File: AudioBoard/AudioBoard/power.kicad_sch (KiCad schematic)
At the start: 3 parts, among them J7 Barrel_Jack, SW3 PWR_SW

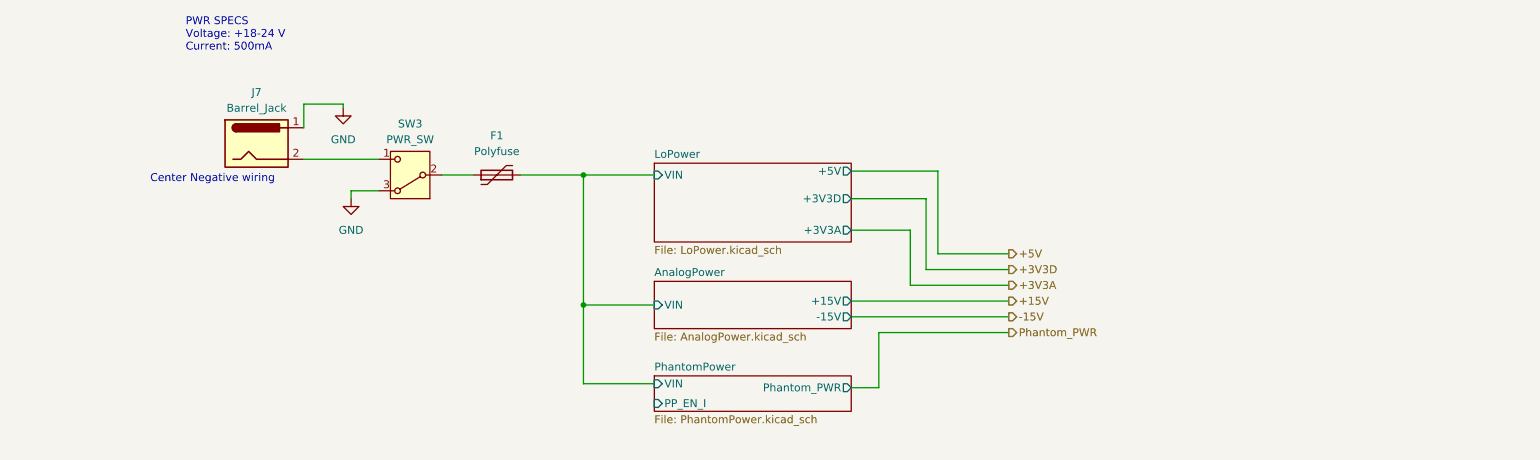
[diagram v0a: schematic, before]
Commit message: added power protection, dcdc modules
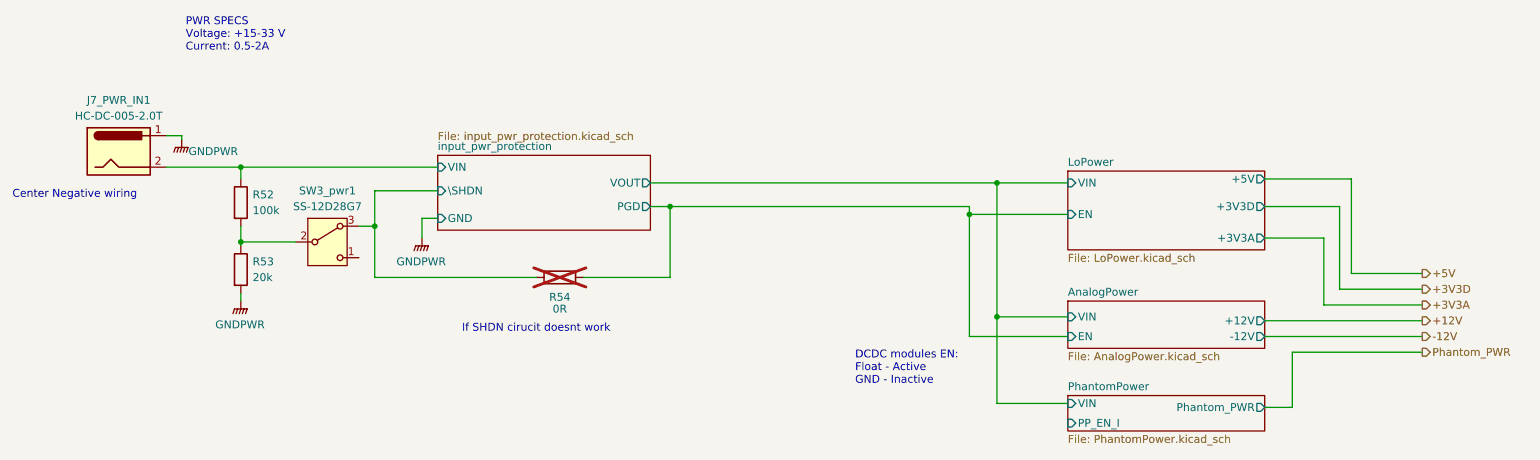
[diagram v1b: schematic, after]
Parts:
- removed F1: Polyfuse, symbol Device:Polyfuse
- added R52: 100k, symbol Device:R
- added R53: 20k, symbol Device:R
- added R54: 0R, symbol Device:R
- J7_PWR_IN1: renamed from J7; value Barrel_Jack -> HC-DC-005-2.0T
- SW3_pwr1: renamed from SW3; value PWR_SW -> SS-12D28G7
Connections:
- net at SW3_pwr1.2 (B): now also R52.2, R53.1
- net at SW3_pwr1.1 (C): no longer J7_PWR_IN1.2
- net GND renamed GNDPWR
- net GNDPWR: now also R53.2; no longer SW3_pwr1.3 (A)
- new net AnalogPower/EN: R54.1
- new net input_pwr_protection/VIN: J7_PWR_IN1.2, R52.1
- new net input_pwr_protection/\SHDN: R54.2, SW3_pwr1.3 (A)
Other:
- added sheet input_pwr_protection (input_pwr_protection.kicad_sch)
- sheet AnalogPower ports: added +12V, -12V, EN; removed +15V, -15V
- sheet LoPower ports: added EN; removed none
- note added: "DCDC modules EN: Float - Active GND - Inactive"
- note added: "If SHDN cirucit doesnt work"
- note added: "PWR SPECS Voltage: +15-33 V Current: 0.5-2A"
- note removed: "PWR SPECS Voltage: +18-24 V Current: 500mA"
- moved on the sheet: J7_PWR_IN1, SW3_pwr1

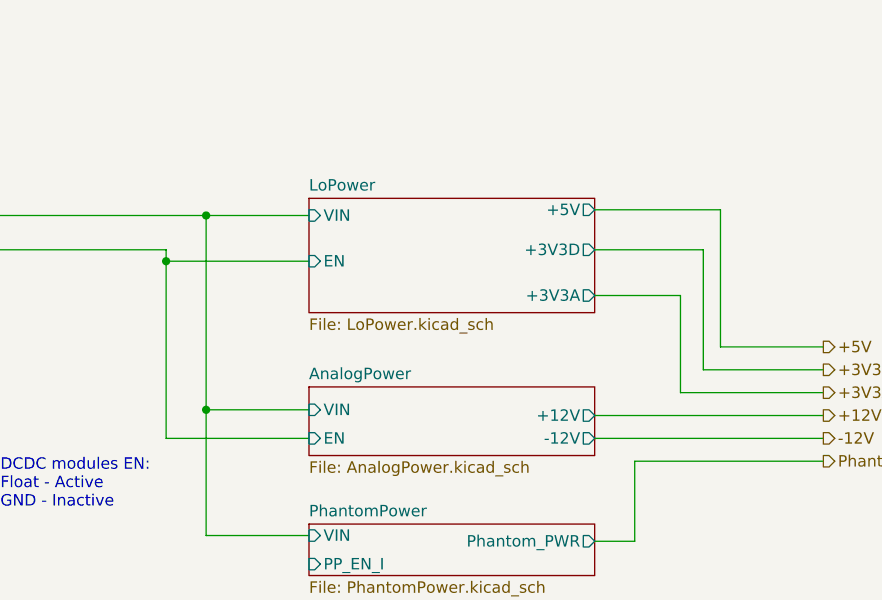
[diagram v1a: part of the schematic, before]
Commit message: assigned footprint to elements lcsc parts
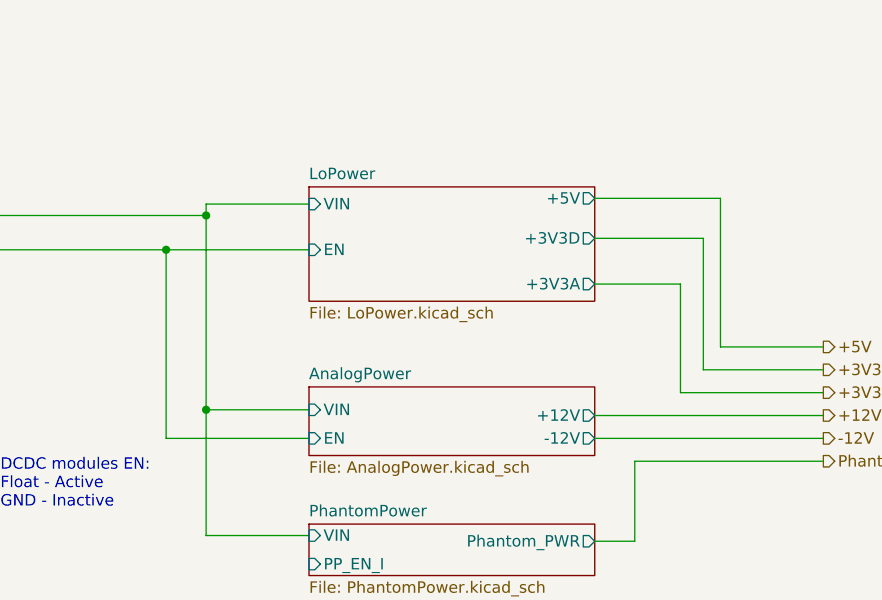
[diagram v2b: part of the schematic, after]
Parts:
- R52: footprint (none) -> Resistor_SMD:R_0402_1005Metric; JLCPCB (none) -> C25741; LCSC Part (none) -> C25741
- R53: footprint (none) -> Resistor_SMD:R_0603_1608Metric; JLCPCB (none) -> C4184; LCSC Part (none) -> C4184
- R54: footprint (none) -> Resistor_SMD:R_0603_1608Metric_Pad0.98x0.95mm_HandSolder; JLCPCB (none) -> C21189; LCSC Part (none) -> C21189
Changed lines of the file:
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@@
+	)
+	(junction
+		(at 174.625 43.815)
+		(diameter 0)
+		(color 0 0 0 0)
 	)
 	(junction
@@
 	)
 	(junction
-		(at 174.625 45.085)
-		(diameter 0)
-		(color 0 0 0 0)
-	)
-	(junction
 		(at 179.07 61.595)
 		(diameter 0)
@@
 	(wire
 		(pts
+			(xy 179.07 38.735) (xy 179.07 40.005)
+		)
+		(stroke
+			(width 0)
+			(type default)
+		)
+	)
+	(wire
+		(pts
 			(xy 57.15 37.465) (xy 57.15 39.37)
 		)
@@
 	(wire
 		(pts
-			(xy 234.315 43.815) (xy 234.315 57.15)
-		)
-		(stroke
-			(width 0)
-			(type default)
-		)
-	)
-	(wire
-		(pts
-			(xy 190.5 45.085) (xy 174.625 45.085)
+			(xy 174.625 43.815) (xy 174.625 64.77)
+		)
+		(stroke
+			(width 0)
+			(type default)
+		)
+	)
+	(wire
+		(pts
+			(xy 234.315 42.545) (xy 234.315 57.15)
+		)
+		(stroke
+			(width 0)
+			(type default)
+		)
+	)
+	(wire
+		(pts
+			(xy 190.5 43.815) (xy 174.625 43.815)
 		)
 		(stroke
@@
 	(wire
 		(pts
-			(xy 236.22 39.37) (xy 222.25 39.37)
+			(xy 236.22 38.1) (xy 222.25 38.1)
 		)
 		(stroke
@@
 	(wire
 		(pts
-			(xy 174.625 45.085) (xy 174.625 64.77)
-		)
-		(stroke
-			(width 0)
-			(type default)
-		)
-	)
-	(wire
-		(pts
-			(xy 174.625 43.815) (xy 174.625 45.085)
-		)
-		(stroke
-			(width 0)
-			(type default)
-		)
-	)
-	(wire
-		(pts
 			(xy 126.365 43.815) (xy 174.625 43.815)
 		)
@@
 	(wire
 		(pts
-			(xy 222.25 43.815) (xy 234.315 43.815)
+			(xy 222.25 42.545) (xy 234.315 42.545)
 		)
 		(stroke
@@
 	(wire
 		(pts
-			(xy 222.25 48.895) (xy 231.775 48.895)
+			(xy 222.25 47.625) (xy 231.775 47.625)
 		)
 		(stroke
@@
 	(wire
 		(pts
-			(xy 179.07 40.005) (xy 190.5 40.005)
+			(xy 179.07 38.735) (xy 190.5 38.735)
 		)
 		(stroke
@@
 	(wire
 		(pts
-			(xy 236.22 54.61) (xy 236.22 39.37)
-		)
-		(stroke
-			(width 0)
-			(type default)
-		)
-	)
-	(wire
-		(pts
-			(xy 231.775 48.895) (xy 231.775 59.69)
+			(xy 236.22 54.61) (xy 236.22 38.1)
+		)
+		(stroke
+			(width 0)
+			(type default)
+		)
+	)
+	(wire
+		(pts
+			(xy 231.775 47.625) (xy 231.775 59.69)
 		)
 		(stroke
@@
 			)
 		)
-		(property "Footprint" ""
+		(property "Footprint" "Resistor_SMD:R_0402_1005Metric"
 			(at 55.372 43.18 90)
 			(hide yes)
@@
 		)
 		(property "Description" "Resistor"
+			(at 57.15 43.18 0)
+			(hide yes)
+			(show_name no)
+			(do_not_autoplace no)
+			(effects
+				(font
+					(size 1.27 1.27)
+				)
+			)
+		)
+		(property "I" ""
+			(at 57.15 43.18 0)
+			(hide yes)
+			(show_name no)
+			(do_not_autoplace no)
+			(effects
+				(font
+					(size 1.27 1.27)
+				)
+			)
+		)
+		(property "JLCPCB" "C25741"
+			(at 57.15 43.18 0)
+			(hide yes)
+			(show_name no)
+			(do_not_autoplace no)
+			(effects
+				(font
+					(size 1.27 1.27)
+				)
+			)
+		)
+		(property "LCSC Part" "C25741"
+			(at 57.15 43.18 0)
+			(hide yes)
+			(show_name no)
+			(do_not_autoplace no)
+			(effects
+				(font
+					(size 1.27 1.27)
+				)
+			)
+		)
+		(property "esr" ""
 			(at 57.15 43.18 0)
 			(hide yes)
@@
 			)
 		)
-		(property "Footprint" ""
+		(property "Footprint" "Resistor_SMD:R_0603_1608Metric"
 			(at 55.372 53.975 90)
 			(hide yes)
@@
 		)
 		(property "Description" "Resistor"
+			(at 57.15 53.975 0)
+			(hide yes)
+			(show_name no)
+			(do_not_autoplace no)
+			(effects
+				(font
+					(size 1.27 1.27)
+				)
+			)
+		)
+		(property "I" ""
+			(at 57.15 53.975 0)
+			(hide yes)
+			(show_name no)
+			(do_not_autoplace no)
+			(effects
+				(font
+					(size 1.27 1.27)
+				)
+			)
+		)
+		(property "JLCPCB" "C4184"
+			(at 57.15 53.975 0)
+			(hide yes)
+			(show_name no)
+			(do_not_autoplace no)
+			(effects
+				(font
+					(size 1.27 1.27)
+				)
+			)
+		)
+		(property "LCSC Part" "C4184"
+			(at 57.15 53.975 0)
+			(hide yes)
+			(show_name no)
+			(do_not_autoplace no)
+			(effects
+				(font
+					(size 1.27 1.27)
+				)
+			)
+		)
+		(property "esr" ""
 			(at 57.15 53.975 0)
 			(hide yes)
@@
 			)
 		)
-		(property "Footprint" ""
+		(property "Footprint" "Resistor_SMD:R_0603_1608Metric_Pad0.98x0.95mm_HandSolder"
 			(at 108.585 53.467 90)
 			(hide yes)
@@
 		(property "Description" "Resistor"
 			(at 108.585 55.245 0)
+			(hide yes)
+			(show_name no)
+			(do_not_autoplace no)
+			(effects
+				(font
+					(size 1.27 1.27)
+				)
+			)
+		)
+		(property "I" ""
+			(at 108.585 55.245 90)
+			(hide yes)
+			(show_name no)
+			(do_not_autoplace no)
+			(effects
+				(font
+					(size 1.27 1.27)
+				)
+			)
+		)
+		(property "esr" ""
+			(at 108.585 55.245 90)
+			(hide yes)
+			(show_name no)
+			(do_not_autoplace no)
+			(effects
+				(font
+					(size 1.27 1.27)
+				)
+			)
+		)
+		(property "JLCPCB" "C21189"
+			(at 108.585 55.245 90)
+			(hide yes)
+			(show_name no)
+			(do_not_autoplace no)
+			(effects
+				(font
+					(size 1.27 1.27)
+				)
+			)
+		)
+		(property "LCSC Part" "C21189"
+			(at 108.585 55.245 90)
 			(hide yes)
 			(show_name no)
@@
 			)
 		)
+		(property "I" ""
+			(at 71.12 49.53 0)
+			(hide yes)
+			(show_name no)
+			(do_not_autoplace no)
+			(effects
+				(font
+					(size 1.27 1.27)
+				)
+			)
+		)
+		(property "esr" ""
+			(at 71.12 49.53 0)
+			(hide yes)
+			(show_name no)
+			(do_not_autoplace no)
+			(effects
+				(font
+					(size 1.27 1.27)
+				)
+			)
+		)
 		(pin "3"
 		)
@@
 			)
 		)
+		(property "I" ""
+			(at 37.465 34.925 0)
+			(hide yes)
+			(show_name no)
+			(do_not_autoplace no)
+			(effects
+				(font
+					(size 1.27 1.27)
+				)
+			)
+		)
+		(property "esr" ""
+			(at 37.465 34.925 0)
+			(hide yes)
+			(show_name no)
+			(do_not_autoplace no)
+			(effects
+				(font
+					(size 1.27 1.27)
+				)
+			)
+		)
 		(pin "1"
 		)
@@
 	)
 	(sheet
-		(at 190.5 38.1)
+		(at 190.5 36.83)
 		(size 31.75 12.7)
 		(exclude_from_sim no)
@@
 		)
 		(property "Sheetname" "LoPower"
-			(at 190.5 37.3884 0)
+			(at 190.5 36.1184 0)
 			(show_name no)
 			(do_not_autoplace no)
@@
 		)
 		(property "Sheetfile" "LoPower.kicad_sch"
-			(at 190.5 51.3846 0)
+			(at 190.5 50.1146 0)
 			(show_name no)
 			(do_not_autoplace no)
@@
 		)
 		(pin "+3V3A" output
-			(at 222.25 48.895 0)
+			(at 222.25 47.625 0)
 			(effects
 				(font
@@
 		)
 		(pin "+3V3D" output
-			(at 222.25 43.815 0)
+			(at 222.25 42.545 0)
 			(effects
 				(font
@@
 		)
 		(pin "+5V" output
-			(at 222.25 39.37 0)
+			(at 222.25 38.1 0)
 			(effects
 				(font
@@
 		)
 		(pin "VIN" input
-			(at 190.5 40.005 180)
+			(at 190.5 38.735 180)
 			(effects
 				(font
@@
 		)
 		(pin "EN" input
-			(at 190.5 45.085 180)
-			(effects
-				(font
+			(at 190.5 43.815 180)
+			(effects
+				(font

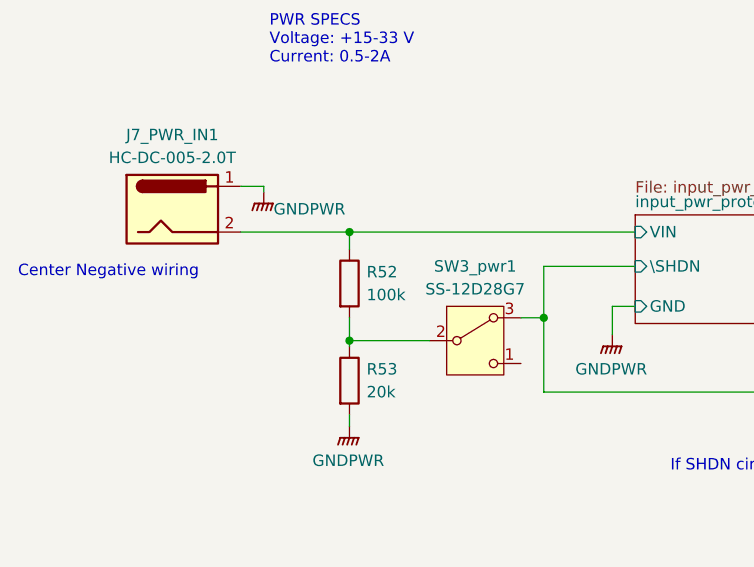
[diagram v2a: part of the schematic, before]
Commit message: added bias voltage buffer, fixed fsw shift reg input filter
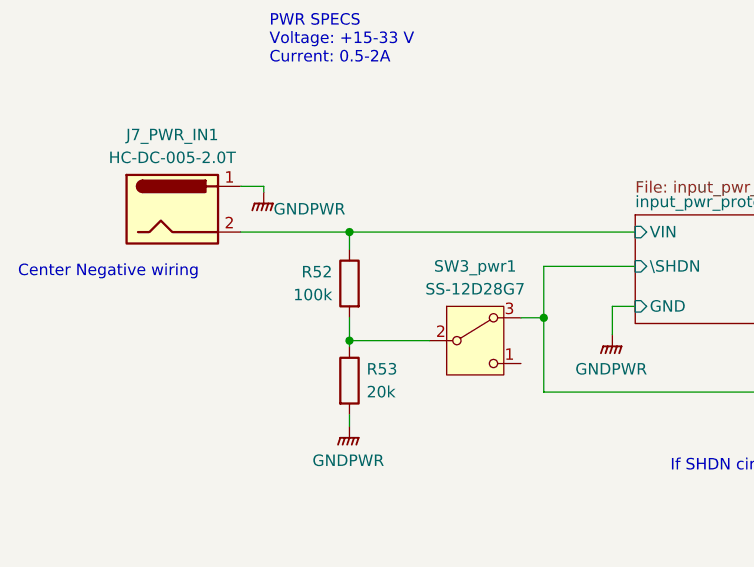
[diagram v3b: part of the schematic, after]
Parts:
- R54: now left out of the parts list
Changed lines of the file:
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@@
 		(lib_id "Device:R")
 		(at 57.15 43.18 0)
+		(mirror y)
 		(unit 1)
 		(body_style 1)
@@
 		(in_pos_files yes)
 		(dnp no)
-		(fields_autoplaced yes)
 		(property "Reference" "R52"
-			(at 59.055 41.9099 0)
+			(at 55.245 41.9099 0)
 			(show_name no)
 			(do_not_autoplace no)
@@
 		)
 		(property "Value" "100k"
-			(at 59.055 44.4499 0)
+			(at 55.245 44.4499 0)
 			(show_name no)
 			(do_not_autoplace no)
@@
 		)
 		(property "Footprint" "Resistor_SMD:R_0402_1005Metric"
-			(at 55.372 43.18 90)
+			(at 58.928 43.18 90)
 			(hide yes)
 			(show_name no)
@@
 		(body_style 1)
 		(exclude_from_sim no)
-		(in_bom yes)
+		(in_bom no)
 		(on_board yes)
 		(in_pos_files yes)

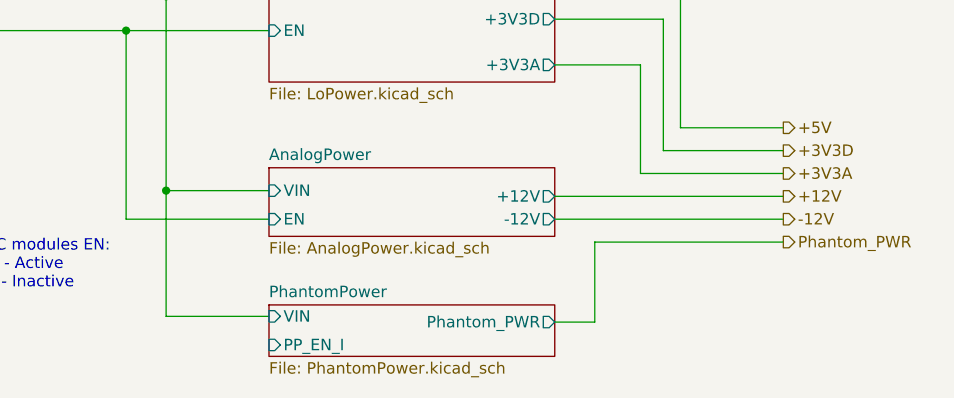
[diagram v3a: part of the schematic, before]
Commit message: modified clamping diodes on inputs, added exp pedal input filter, added ideas to instrument input filter redesign
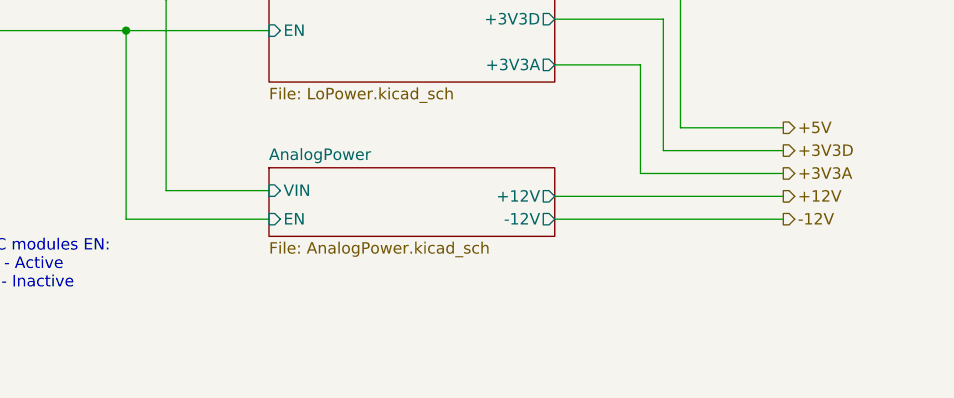
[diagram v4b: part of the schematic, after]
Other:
- removed sheet PhantomPower
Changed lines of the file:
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@@
-	)
-	(junction
-		(at 179.07 61.595)
-		(diameter 0)
-		(color 0 0 0 0)
 	)
 	(junction
@@
 	(wire
 		(pts
-			(xy 179.07 75.565) (xy 190.5 75.565)
-		)
-		(stroke
-			(width 0)
-			(type default)
-		)
-	)
-	(wire
-		(pts
 			(xy 78.74 41.275) (xy 78.74 46.99)
 		)
@@
 	(wire
 		(pts
-			(xy 222.25 76.2) (xy 226.695 76.2)
-		)
-		(stroke
-			(width 0)
-			(type default)
-		)
-	)
-	(wire
-		(pts
 			(xy 126.365 55.245) (xy 126.365 43.815)
 		)
@@
 	(wire
 		(pts
-			(xy 226.695 76.2) (xy 226.695 67.31)
-		)
-		(stroke
-			(width 0)
-			(type default)
-		)
-	)
-	(wire
-		(pts
 			(xy 179.07 61.595) (xy 190.5 61.595)
 		)
@@
 	(wire
 		(pts
-			(xy 226.695 67.31) (xy 247.65 67.31)
-		)
-		(stroke
-			(width 0)
-			(type default)
-		)
-	)
-	(wire
-		(pts
 			(xy 174.625 43.815) (xy 174.625 64.77)
 		)
@@
 		(pts
 			(xy 45.085 32.385) (xy 47.625 32.385)
-		)
-		(stroke
-			(width 0)
-			(type default)
-		)
-	)
-	(wire
-		(pts
-			(xy 179.07 61.595) (xy 179.07 75.565)
 		)
 		(stroke
@@
 		(shape output)
 		(at 247.65 54.61 0)
-		(effects
-			(font
-				(size 1.27 1.27)
-			)
-			(justify left)
-		)
-	)
-	(hierarchical_label "Phantom_PWR"
-		(shape output)
-		(at 247.65 67.31 0)
 		(effects
 			(font
@@
 				)
 			)
-		)
-	)
-	(sheet
-		(at 190.5 74.295)
-		(size 31.75 5.715)
-		(exclude_from_sim no)
-		(in_bom yes)
-		(on_board yes)
-		(dnp no)
-		(fields_autoplaced yes)
-		(stroke
-			(width 0.1524)
-			(type solid)
-		)
-		(fill
-			(color 0 0 0 0)
-		)
-		(property "Sheetname" "PhantomPower"
-			(at 190.5 73.5834 0)
-			(show_name no)
-			(do_not_autoplace no)
-			(effects
-				(font
-					(size 1.27 1.27)
-				)
-				(justify left bottom)
-			)
-		)
-		(property "Sheetfile" "PhantomPower.kicad_sch"
-			(at 190.5 80.5946 0)
-			(show_name no)
-			(do_not_autoplace no)
-			(effects
-				(font
-					(size 1.27 1.27)
-				)
-				(justify left top)
-			)
-		)
-		(pin "VIN" input
-			(at 190.5 75.565 180)
-			(effects
-				(font
-					(size 1.27 1.27)
-				)
-				(justify left)
-			)
-		)
-		(pin "PP_EN_I" input
-			(at 190.5 78.74 180)
-			(effects
-				(font
-					(size 1.27 1.27)
-				)
-				(justify left)
-			)
-		)
-		(pin "Phantom_PWR" output
-			(at 222.25 76.2 0)
-			(effects
-				(font
-					(size 1.27 1.27)
-				)
-				(justify right)
-			)
-		)
-		(instances
-			(project "AudioBoard"
-				(path "/dd5d876d-fff7-4cb4-baee-a023036d12ae/ee404ad0-726e-426f-8607-a7730f1919f6"
-					(page "20")
-				)
-			)
